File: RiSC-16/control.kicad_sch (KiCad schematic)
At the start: 9 parts, among them U16 74LS373, U17 74LS257, U18 74LS257, U2 74LS373

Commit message: Added a custom symbol for the AM29705. Reworked to use it in two different approaches.
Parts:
- renumbered C13 to C15, C14 to C16, C15 to C17, C16 to C18, R1 to R3, U2 to U15, U17 to U16, U16 to U17
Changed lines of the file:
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@@
 		)
 	)
-	(global_label "SRC1[0..2]"
+	(global_label "SRC1[0..3]"
 		(shape input)
 		(at 100.33 119.38 0)
@@
 		)
 	)
-	(global_label "TGT[0..2]"
+	(global_label "TGT[0..3]"
 		(shape input)
 		(at 100.33 148.59 0)
@@
 		)
 	)
-	(global_label "SRC2[0..2]"
+	(global_label "SRC2[0..3]"
 		(shape input)
 		(at 177.8 129.54 0)
@@
 		(dnp no)
 		(fields_autoplaced yes)
-		(property "Reference" "C13"
+		(property "Reference" "C15"
 			(at 182.88 153.7969 0)
 			(effects
@@
 			(project "RiSC-16"
 				(path "/09ce4153-429f-4803-b069-3af485a81dd6/bf059c65-0001-4da1-977b-c7ca81f82c3a"
-					(reference "C13")
+					(reference "C15")
 					(unit 1)
 				)
@@
 		(dnp no)
 		(fields_autoplaced yes)
-		(property "Reference" "U17"
+		(property "Reference" "U16"
 			(at 154.5433 60.96 0)
 			(effects
@@
 			(project "RiSC-16"
 				(path "/09ce4153-429f-4803-b069-3af485a81dd6/bf059c65-0001-4da1-977b-c7ca81f82c3a"
-					(reference "U17")
+					(reference "U16")
 					(unit 1)
 				)
@@
 		(dnp no)
 		(fields_autoplaced yes)
-		(property "Reference" "#PWR044"
+		(property "Reference" "#PWR047"
 			(at 180.34 163.83 0)
 			(effects
@@
 			(project "RiSC-16"
 				(path "/09ce4153-429f-4803-b069-3af485a81dd6/bf059c65-0001-4da1-977b-c7ca81f82c3a"
-					(reference "#PWR044")
+					(reference "#PWR047")
 					(unit 1)
 				)
@@
 		(dnp no)
 		(fields_autoplaced yes)
-		(property "Reference" "#PWR030"
+		(property "Reference" "#PWR040"
 			(at 180.34 86.36 0)
 			(effects
@@
 			(project ""
 				(path "/09ce4153-429f-4803-b069-3af485a81dd6/bf059c65-0001-4da1-977b-c7ca81f82c3a"
-					(reference "#PWR030")
+					(reference "#PWR040")
 					(unit 1)
 				)
@@
 		(dnp no)
 		(fields_autoplaced yes)
-		(property "Reference" "#PWR032"
+		(property "Reference" "#PWR044"
 			(at 152.4 128.27 0)
 			(effects
@@
 			(project ""
 				(path "/09ce4153-429f-4803-b069-3af485a81dd6/bf059c65-0001-4da1-977b-c7ca81f82c3a"
-					(reference "#PWR032")
+					(reference "#PWR044")
 					(unit 1)
 				)
@@
 		(dnp no)
 		(fields_autoplaced yes)
-		(property "Reference" "#PWR043"
+		(property "Reference" "#PWR045"
 			(at 180.34 156.21 0)
 			(effects
@@
 			(project "RiSC-16"
 				(path "/09ce4153-429f-4803-b069-3af485a81dd6/bf059c65-0001-4da1-977b-c7ca81f82c3a"
-					(reference "#PWR043")
+					(reference "#PWR045")
 					(unit 1)
 				)
@@
 		(dnp no)
 		(fields_autoplaced yes)
-		(property "Reference" "C14"
+		(property "Reference" "C16"
 			(at 195.58 153.7969 0)
 			(effects
@@
 			(project "RiSC-16"
 				(path "/09ce4153-429f-4803-b069-3af485a81dd6/bf059c65-0001-4da1-977b-c7ca81f82c3a"
-					(reference "C14")
+					(reference "C16")
 					(unit 1)
 				)
@@
 		(dnp no)
 		(fields_autoplaced yes)
-		(property "Reference" "U16"
+		(property "Reference" "U17"
 			(at 58.0233 116.84 0)
 			(effects
@@
 			(project ""
 				(path "/09ce4153-429f-4803-b069-3af485a81dd6/bf059c65-0001-4da1-977b-c7ca81f82c3a"
-					(reference "U16")
+					(reference "U17")
 					(unit 1)
 				)
@@
 		(dnp no)
 		(fields_autoplaced yes)
-		(property "Reference" "C16"
+		(property "Reference" "C18"
 			(at 220.98 153.7969 0)
 			(effects
@@
 			(project "RiSC-16"
 				(path "/09ce4153-429f-4803-b069-3af485a81dd6/bf059c65-0001-4da1-977b-c7ca81f82c3a"
-					(reference "C16")
+					(reference "C18")
 					(unit 1)
 				)
@@
 		(dnp no)
 		(fields_autoplaced yes)
-		(property "Reference" "C15"
+		(property "Reference" "C17"
 			(at 208.28 153.7969 0)
 			(effects
@@
 			(project "RiSC-16"
 				(path "/09ce4153-429f-4803-b069-3af485a81dd6/bf059c65-0001-4da1-977b-c7ca81f82c3a"
-					(reference "C15")
+					(reference "C17")
 					(unit 1)
 				)
@@
 		(dnp no)
 		(fields_autoplaced yes)
-		(property "Reference" "#PWR031"
+		(property "Reference" "#PWR043"
 			(at 55.88 120.65 0)
 			(effects
@@
 			(project ""
 				(path "/09ce4153-429f-4803-b069-3af485a81dd6/bf059c65-0001-4da1-977b-c7ca81f82c3a"
-					(reference "#PWR031")
+					(reference "#PWR043")
 					(unit 1)
 				)
@@
 		(dnp no)
 		(fields_autoplaced yes)
-		(property "Reference" "#PWR026"
+		(property "Reference" "#PWR041"
 			(at 55.88 100.33 0)
 			(effects
@@
 			(project ""
 				(path "/09ce4153-429f-4803-b069-3af485a81dd6/bf059c65-0001-4da1-977b-c7ca81f82c3a"
-					(reference "#PWR026")
+					(reference "#PWR041")
 					(unit 1)
 				)
@@
 		(dnp no)
 		(fields_autoplaced yes)
-		(property "Reference" "#PWR028"
+		(property "Reference" "#PWR038"
 			(at 152.4 64.77 0)
 			(effects
@@
 			(project "RiSC-16"
 				(path "/09ce4153-429f-4803-b069-3af485a81dd6/bf059c65-0001-4da1-977b-c7ca81f82c3a"
-					(reference "#PWR028")
+					(reference "#PWR038")
 					(unit 1)
 				)
@@
 		(dnp no)
 		(fields_autoplaced yes)
-		(property "Reference" "#PWR029"
+		(property "Reference" "#PWR042"
 			(at 152.4 115.57 0)
 			(effects
@@
 			(project "RiSC-16"
 				(path "/09ce4153-429f-4803-b069-3af485a81dd6/bf059c65-0001-4da1-977b-c7ca81f82c3a"
-					(reference "#PWR029")
+					(reference "#PWR042")
 					(unit 1)
 				)
@@
 		(dnp no)
 		(fields_autoplaced yes)
-		(property "Reference" "#PWR027"
+		(property "Reference" "#PWR039"
 			(at 180.34 72.39 0)
 			(effects
@@
 			(project ""
 				(path "/09ce4153-429f-4803-b069-3af485a81dd6/bf059c65-0001-4da1-977b-c7ca81f82c3a"
-					(reference "#PWR027")
+					(reference "#PWR039")
 					(unit 1)
 				)
@@
 		(dnp no)
 		(fields_autoplaced yes)
-		(property "Reference" "U2"
+		(property "Reference" "U15"
 			(at 58.0233 53.34 0)
 			(effects
@@
 			(project ""
 				(path "/09ce4153-429f-4803-b069-3af485a81dd6/bf059c65-0001-4da1-977b-c7ca81f82c3a"
-					(reference "U2")
+					(reference "U15")
 					(unit 1)
 				)
@@
 		(dnp no)
 		(fields_autoplaced yes)
-		(property "Reference" "#PWR041"
+		(property "Reference" "#PWR046"
 			(at 55.88 163.83 0)
 			(effects
@@
 			(project ""
 				(path "/09ce4153-429f-4803-b069-3af485a81dd6/bf059c65-0001-4da1-977b-c7ca81f82c3a"
-					(reference "#PWR041")
+					(reference "#PWR046")
 					(unit 1)
 				)
@@
 		(dnp no)
 		(fields_autoplaced yes)
-		(property "Reference" "R1"
+		(property "Reference" "R3"
 			(at 182.88 69.8499 0)
 			(effects
@@
 			(project ""
 				(path "/09ce4153-429f-4803-b069-3af485a81dd6/bf059c65-0001-4da1-977b-c7ca81f82c3a"
-					(reference "R1")
+					(reference "R3")
 					(unit 1)
 				)
@@
 		(dnp no)
 		(fields_autoplaced yes)
-		(property "Reference" "#PWR042"
+		(property "Reference" "#PWR048"
 			(at 152.4 179.07 0)
 			(effects
@@
 			(project ""
 				(path "/09ce4153-429f-4803-b069-3af485a81dd6/bf059c65-0001-4da1-977b-c7ca81f82c3a"
-					(reference "#PWR042")
-					(unit 1)
-				)
+					(reference "#PWR048")
+					(unit 1)
+				)

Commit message: Check point of design.
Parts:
- renumbered C15 to C18, C16 to C19, C17 to C20, C18 to C21, R3 to R4, U15 to U18, U16 to U19, U17 to U20, U18 to U21
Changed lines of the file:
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@@
 		(dnp no)
 		(fields_autoplaced yes)
-		(property "Reference" "C15"
+		(property "Reference" "C18"
 			(at 182.88 153.7969 0)
 			(effects
@@
 			(project "RiSC-16"
 				(path "/09ce4153-429f-4803-b069-3af485a81dd6/bf059c65-0001-4da1-977b-c7ca81f82c3a"
-					(reference "C15")
+					(reference "C18")
 					(unit 1)
 				)
@@
 		(dnp no)
 		(fields_autoplaced yes)
-		(property "Reference" "U16"
+		(property "Reference" "U19"
 			(at 154.5433 60.96 0)
 			(effects
@@
 			(project "RiSC-16"
 				(path "/09ce4153-429f-4803-b069-3af485a81dd6/bf059c65-0001-4da1-977b-c7ca81f82c3a"
-					(reference "U16")
+					(reference "U19")
 					(unit 1)
 				)
@@
 		(dnp no)
 		(fields_autoplaced yes)
-		(property "Reference" "#PWR047"
+		(property "Reference" "#PWR053"
 			(at 180.34 163.83 0)
 			(effects
@@
 			(project "RiSC-16"
 				(path "/09ce4153-429f-4803-b069-3af485a81dd6/bf059c65-0001-4da1-977b-c7ca81f82c3a"
-					(reference "#PWR047")
+					(reference "#PWR053")
 					(unit 1)
 				)
@@
 		(dnp no)
 		(fields_autoplaced yes)
-		(property "Reference" "#PWR040"
+		(property "Reference" "#PWR046"
 			(at 180.34 86.36 0)
 			(effects
@@
 			(project ""
 				(path "/09ce4153-429f-4803-b069-3af485a81dd6/bf059c65-0001-4da1-977b-c7ca81f82c3a"
-					(reference "#PWR040")
+					(reference "#PWR046")
 					(unit 1)
 				)
@@
 		(dnp no)
 		(fields_autoplaced yes)
-		(property "Reference" "#PWR044"
+		(property "Reference" "#PWR050"
 			(at 152.4 128.27 0)
 			(effects
@@
 			(project ""
 				(path "/09ce4153-429f-4803-b069-3af485a81dd6/bf059c65-0001-4da1-977b-c7ca81f82c3a"
-					(reference "#PWR044")
+					(reference "#PWR050")
 					(unit 1)
 				)
@@
 		(dnp no)
 		(fields_autoplaced yes)
-		(property "Reference" "#PWR045"
+		(property "Reference" "#PWR051"
 			(at 180.34 156.21 0)
 			(effects
@@
 			(project "RiSC-16"
 				(path "/09ce4153-429f-4803-b069-3af485a81dd6/bf059c65-0001-4da1-977b-c7ca81f82c3a"
-					(reference "#PWR045")
+					(reference "#PWR051")
 					(unit 1)
 				)
@@
 		(dnp no)
 		(fields_autoplaced yes)
-		(property "Reference" "C16"
+		(property "Reference" "C19"
 			(at 195.58 153.7969 0)
 			(effects
@@
 			(project "RiSC-16"
 				(path "/09ce4153-429f-4803-b069-3af485a81dd6/bf059c65-0001-4da1-977b-c7ca81f82c3a"
-					(reference "C16")
+					(reference "C19")
 					(unit 1)
 				)
@@
 		(dnp no)
 		(fields_autoplaced yes)
-		(property "Reference" "U17"
+		(property "Reference" "U20"
 			(at 58.0233 116.84 0)
 			(effects
@@
 			(project ""
 				(path "/09ce4153-429f-4803-b069-3af485a81dd6/bf059c65-0001-4da1-977b-c7ca81f82c3a"
-					(reference "U17")
+					(reference "U20")
 					(unit 1)
 				)
@@
 		(dnp no)
 		(fields_autoplaced yes)
-		(property "Reference" "C18"
+		(property "Reference" "C21"
 			(at 220.98 153.7969 0)
 			(effects
@@
 			(project "RiSC-16"
 				(path "/09ce4153-429f-4803-b069-3af485a81dd6/bf059c65-0001-4da1-977b-c7ca81f82c3a"
-					(reference "C18")
+					(reference "C21")
 					(unit 1)
 				)
@@
 		(dnp no)
 		(fields_autoplaced yes)
-		(property "Reference" "C17"
+		(property "Reference" "C20"
 			(at 208.28 153.7969 0)
 			(effects
@@
 			(project "RiSC-16"
 				(path "/09ce4153-429f-4803-b069-3af485a81dd6/bf059c65-0001-4da1-977b-c7ca81f82c3a"
-					(reference "C17")
+					(reference "C20")
 					(unit 1)
 				)
@@
 		(dnp no)
 		(fields_autoplaced yes)
-		(property "Reference" "#PWR043"
+		(property "Reference" "#PWR049"
 			(at 55.88 120.65 0)
 			(effects
@@
 			(project ""
 				(path "/09ce4153-429f-4803-b069-3af485a81dd6/bf059c65-0001-4da1-977b-c7ca81f82c3a"
-					(reference "#PWR043")
+					(reference "#PWR049")
 					(unit 1)
 				)
@@
 		(dnp no)
 		(fields_autoplaced yes)
-		(property "Reference" "U18"
+		(property "Reference" "U21"
 			(at 154.5433 124.46 0)
 			(effects
@@
 			(project "RiSC-16"
 				(path "/09ce4153-429f-4803-b069-3af485a81dd6/bf059c65-0001-4da1-977b-c7ca81f82c3a"
-					(reference "U18")
+					(reference "U21")
 					(unit 1)
 				)
@@
 		(dnp no)
 		(fields_autoplaced yes)
-		(property "Reference" "#PWR041"
+		(property "Reference" "#PWR047"
 			(at 55.88 100.33 0)
 			(effects
@@
 			(project ""
 				(path "/09ce4153-429f-4803-b069-3af485a81dd6/bf059c65-0001-4da1-977b-c7ca81f82c3a"
-					(reference "#PWR041")
+					(reference "#PWR047")
 					(unit 1)
 				)
@@
 		(dnp no)
 		(fields_autoplaced yes)
-		(property "Reference" "#PWR038"
+		(property "Reference" "#PWR044"
 			(at 152.4 64.77 0)
 			(effects
@@
 			(project "RiSC-16"
 				(path "/09ce4153-429f-4803-b069-3af485a81dd6/bf059c65-0001-4da1-977b-c7ca81f82c3a"
-					(reference "#PWR038")
+					(reference "#PWR044")
 					(unit 1)
 				)
@@
 		(dnp no)
 		(fields_autoplaced yes)
-		(property "Reference" "#PWR042"
+		(property "Reference" "#PWR048"
 			(at 152.4 115.57 0)
 			(effects
@@
 			(project "RiSC-16"
 				(path "/09ce4153-429f-4803-b069-3af485a81dd6/bf059c65-0001-4da1-977b-c7ca81f82c3a"
-					(reference "#PWR042")
+					(reference "#PWR048")
 					(unit 1)
 				)
@@
 		(dnp no)
 		(fields_autoplaced yes)
-		(property "Reference" "#PWR039"
+		(property "Reference" "#PWR045"
 			(at 180.34 72.39 0)
 			(effects
@@
 			(project ""
 				(path "/09ce4153-429f-4803-b069-3af485a81dd6/bf059c65-0001-4da1-977b-c7ca81f82c3a"
-					(reference "#PWR039")
+					(reference "#PWR045")
 					(unit 1)
 				)
@@
 		(dnp no)
 		(fields_autoplaced yes)
-		(property "Reference" "U15"
+		(property "Reference" "U18"
 			(at 58.0233 53.34 0)
 			(effects
@@
 			(project ""
 				(path "/09ce4153-429f-4803-b069-3af485a81dd6/bf059c65-0001-4da1-977b-c7ca81f82c3a"
-					(reference "U15")
+					(reference "U18")
 					(unit 1)
 				)
@@
 		(dnp no)
 		(fields_autoplaced yes)
-		(property "Reference" "#PWR046"
+		(property "Reference" "#PWR052"
 			(at 55.88 163.83 0)
 			(effects
@@
 			(project ""
 				(path "/09ce4153-429f-4803-b069-3af485a81dd6/bf059c65-0001-4da1-977b-c7ca81f82c3a"
-					(reference "#PWR046")
+					(reference "#PWR052")
 					(unit 1)
 				)
@@
 		(dnp no)
 		(fields_autoplaced yes)
-		(property "Reference" "R3"
+		(property "Reference" "R4"
 			(at 182.88 69.8499 0)
 			(effects
@@
 			(project ""
 				(path "/09ce4153-429f-4803-b069-3af485a81dd6/bf059c65-0001-4da1-977b-c7ca81f82c3a"
-					(reference "R3")
+					(reference "R4")
 					(unit 1)
 				)
@@
 		(dnp no)
 		(fields_autoplaced yes)
-		(property "Reference" "#PWR048"
+		(property "Reference" "#PWR054"
 			(at 152.4 179.07 0)
 			(effects
@@
 			(project ""
 				(path "/09ce4153-429f-4803-b069-3af485a81dd6/bf059c65-0001-4da1-977b-c7ca81f82c3a"
-					(reference "#PWR048")
-					(unit 1)
-				)
+					(reference "#PWR054")
+					(unit 1)
+				)

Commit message: Moved and renamed pages.
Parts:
- removed C18, C19, C20, C21: 0.1 uF, symbol Device:C_Small_US
- removed R4: 5k, symbol Device:R_Small_US
- removed U18, U20: 74LS373, symbol 74xx:74LS373
- removed U19, U21: 74LS257, symbol 74xx:74LS257
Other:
- note removed: "Instruction Register"
- note removed: "Place decoupling capacitors near each IC."
- note removed: "These are the required control bits for the ALU. Cn S0 S1 S2 S3 M 1 0 0 0 0 0 A 1 1 0 0 1 0 A plus B X 0 1 0 0 1 A nand B Cn is hardwired to 1 S2 is hardwired to 0 MUXalu3 is a microcode ROM control signal. It select the source of ALU function. ALU0, ALU1, ALU2, ALU3 are encoded in ALU instruction. FUNCalu0, FUNCalu1, FUNCalu2, FUNCalu3 come from microcode."

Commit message: Refined instruction register.
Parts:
- added R2: 5k, symbol Device:R_Small_US
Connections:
- new net +5V: R2.1
- new net ALUcn: R2.2
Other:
- note added: "These are the required control bits for the ALU. Cn S0 S1 S2 S3 M 1 0 0 0 0 0 A 1 1 0 0 1 0 A plus B X 0 1 0 0 1 A nand B Cn is hardwired to 1 S2 is hardwired to 0 MUXalu3 is a microcode ROM control signal. It select the source of ALU function. ALU0, ALU1, ALU2, ALU3 are encoded in ALU instruction. FUNCalu0, FUNCalu1, FUNCalu2, FUNCalu3 come from microcode."

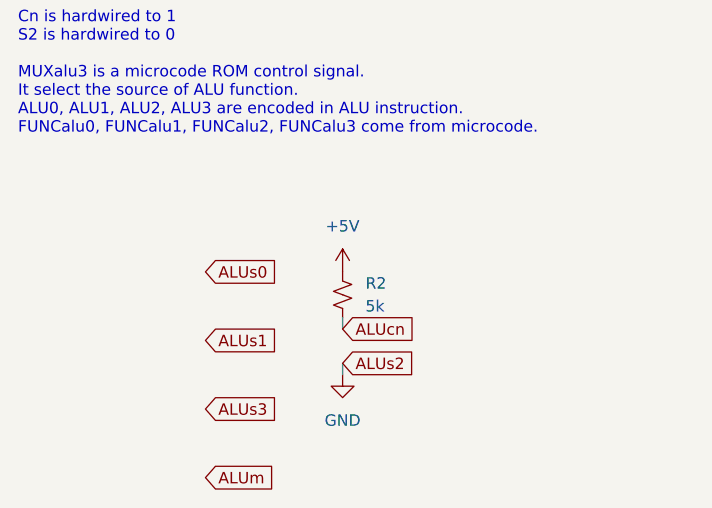
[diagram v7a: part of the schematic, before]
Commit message: Annotated the schematic to align part numbers. EPROM and RAM board was added last revision. Reworked the src1 latching to assert 0xf to select the PC.
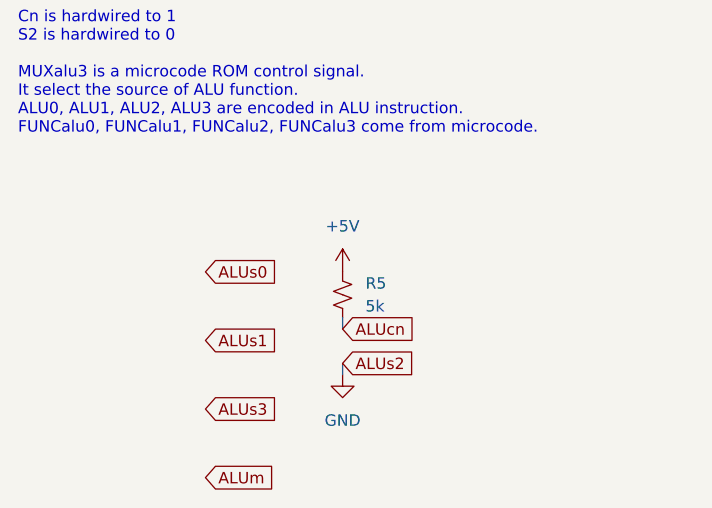
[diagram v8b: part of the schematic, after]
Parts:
- renumbered R2 to R5
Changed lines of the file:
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@@
 		(dnp no)
 		(fields_autoplaced yes)
-		(property "Reference" "R2"
+		(property "Reference" "R5"
 			(at 266.7 59.6899 0)
 			(effects
@@
 			(project "RiSC-16"
 				(path "/09ce4153-429f-4803-b069-3af485a81dd6/bf059c65-0001-4da1-977b-c7ca81f82c3a"
-					(reference "R2")
+					(reference "R5")
 					(unit 1)
 				)
@@
 		(dnp no)
 		(fields_autoplaced yes)
-		(property "Reference" "#PWR016"
+		(property "Reference" "#PWR051"
 			(at 264.16 76.2 0)
 			(effects
@@
 			(project "RiSC-16"
 				(path "/09ce4153-429f-4803-b069-3af485a81dd6/bf059c65-0001-4da1-977b-c7ca81f82c3a"
-					(reference "#PWR016")
+					(reference "#PWR051")
 					(unit 1)
 				)
@@
 		(dnp no)
 		(fields_autoplaced yes)
-		(property "Reference" "#PWR015"
+		(property "Reference" "#PWR050"
 			(at 264.16 62.23 0)
 			(effects
@@
 			(project "RiSC-16"
 				(path "/09ce4153-429f-4803-b069-3af485a81dd6/bf059c65-0001-4da1-977b-c7ca81f82c3a"
-					(reference "#PWR015")
+					(reference "#PWR050")
 					(unit 1)
 				)
